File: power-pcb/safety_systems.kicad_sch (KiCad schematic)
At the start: 54 parts, among them J12 Conn_01x06, J13 Conn_01x03, J14 Conn_01x05, J15 Conn_01x02, J16 Conn_01x06, J17 Screw_Terminal_01x04, J18 Screw_Terminal_01x02, K1 G5Q-1A, K2 G5Q-1A, Q1 AO3400A, Q2 AO3400A, Q3 AO3400A, U22 SN65HVD230, U23 74AHC1G08

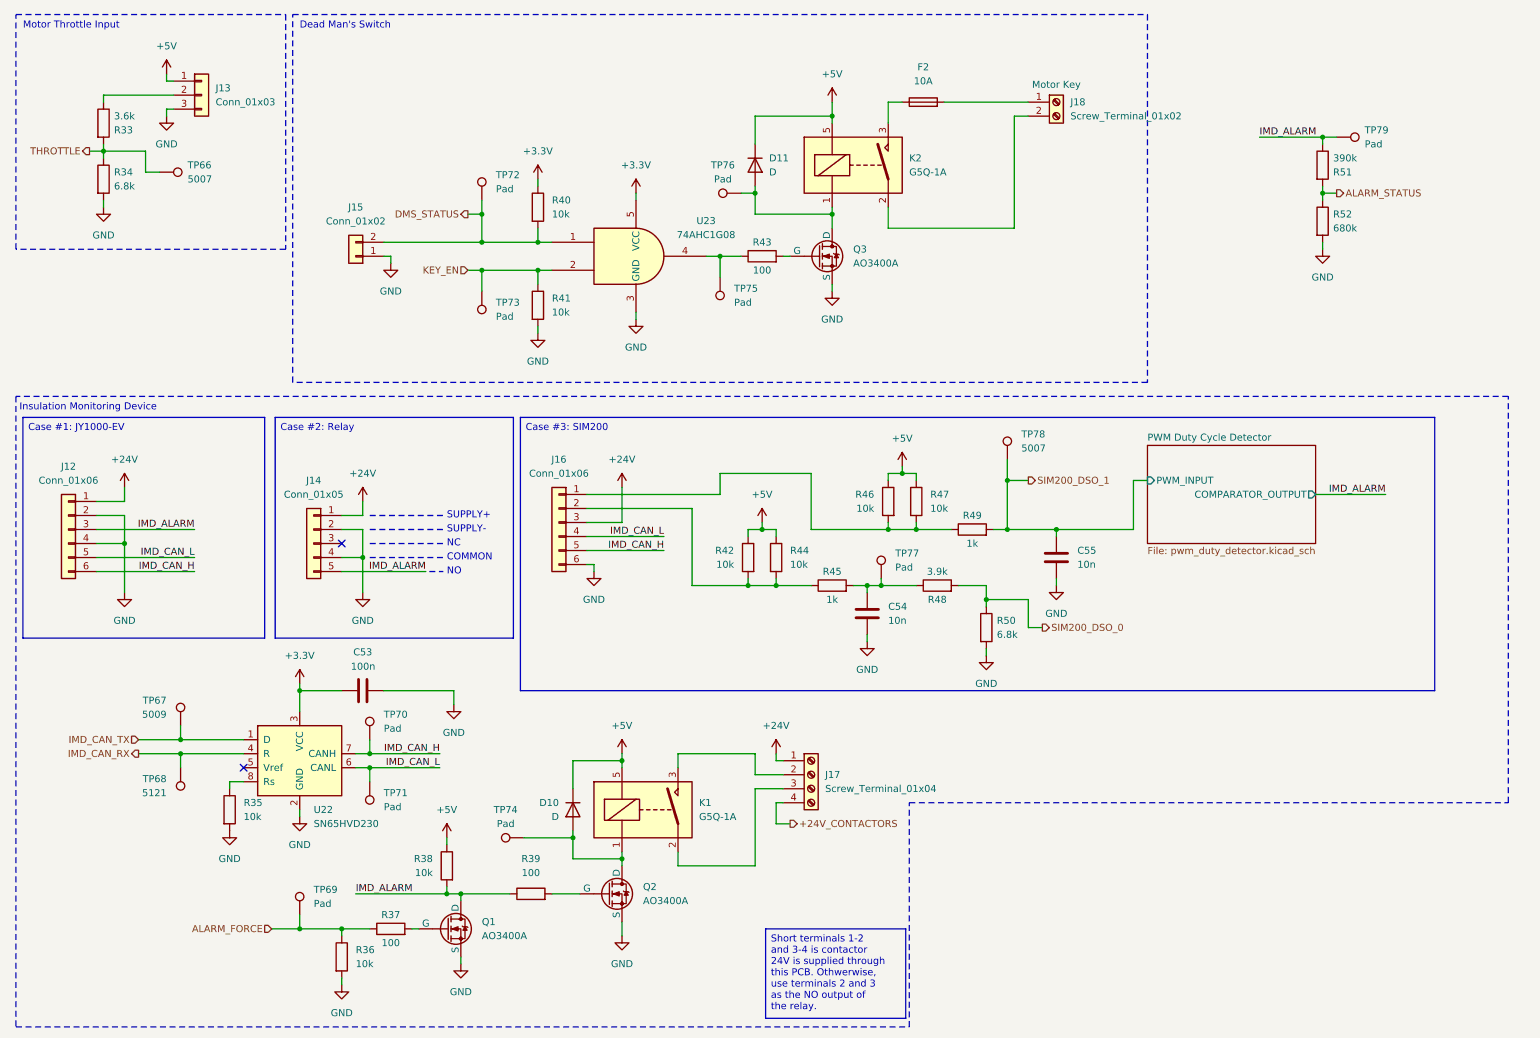
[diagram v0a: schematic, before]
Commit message: power-pcb: finish schematic pages 1 to 7
- overview
- non-isolated interfaces + power
- stm32 microcontroller
- relay board connection
- battery sensors
- 48v i-v sensing (x2)
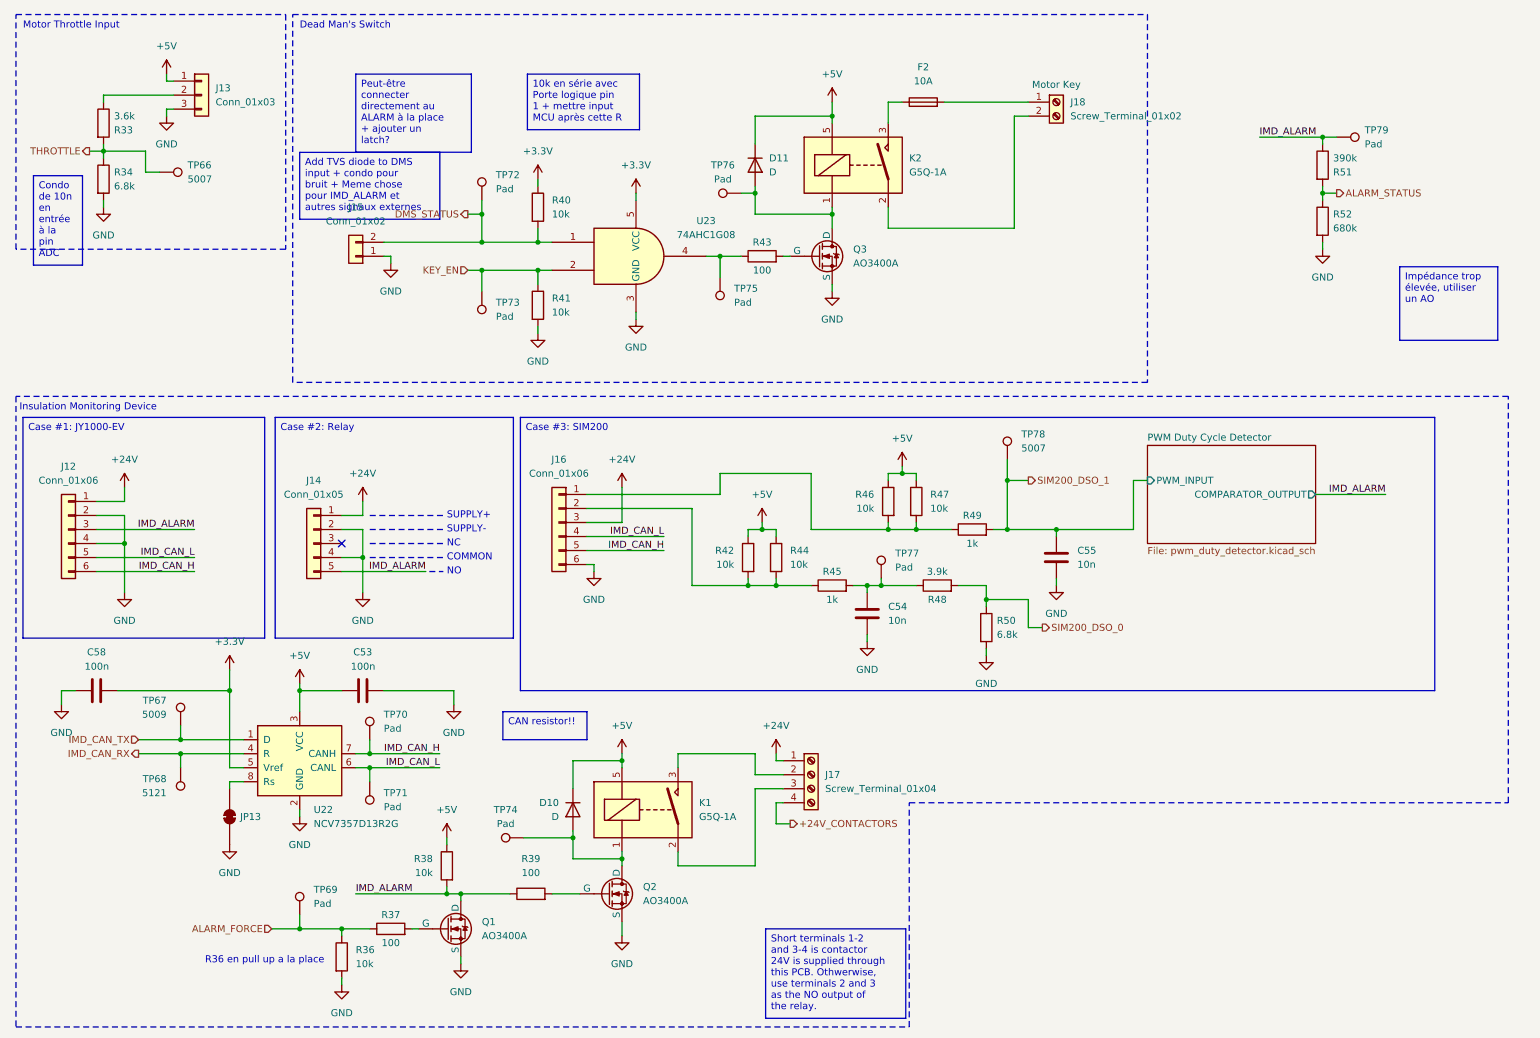
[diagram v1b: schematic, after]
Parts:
- removed R35: 10k, Resistor_SMD:R_0402_1005Metric, symbol Device:R
- added C58: 100n, Capacitor_SMD:C_0603_1608Metric_Pad1.08x0.95mm_HandSolder, symbol Device:C
- added JP13: SolderJumper_2_Bridged, symbol Jumper:SolderJumper_2_Bridged
- U22: value SN65HVD230 -> NCV7357D13R2G; JLCPCB C12084 -> C603987
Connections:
- net +3.3V: now also U22.5 (Vref), C58.1; no longer C53.2, U22.3 (VCC)
- net +5V: now also C53.2, U22.3 (VCC)
- net GND: now also C58.2, JP13.1 (A)
- net at U22.8 (Rs): now also JP13.2 (B)
- no-connect marks 2 -> 1
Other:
- note added: "R36 en pull up a la place"

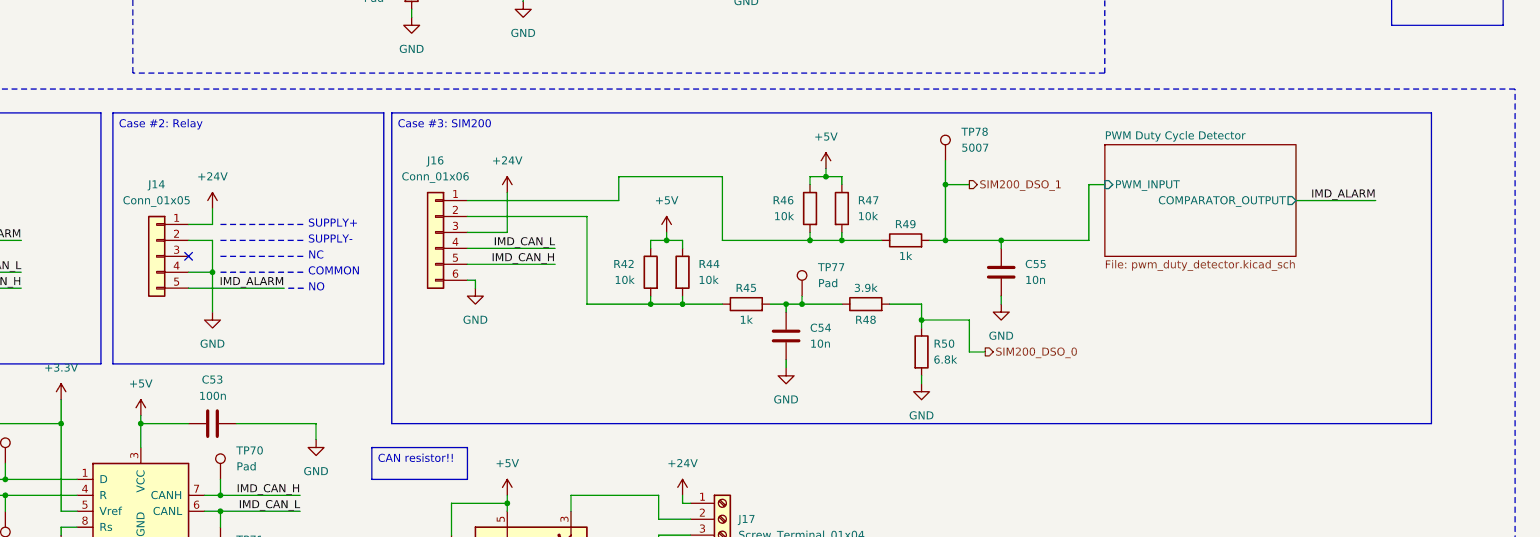
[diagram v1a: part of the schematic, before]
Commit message: power-pcb: remove unused sheets
After renaming, KiCad left the old sheets, but they were never
referenced.
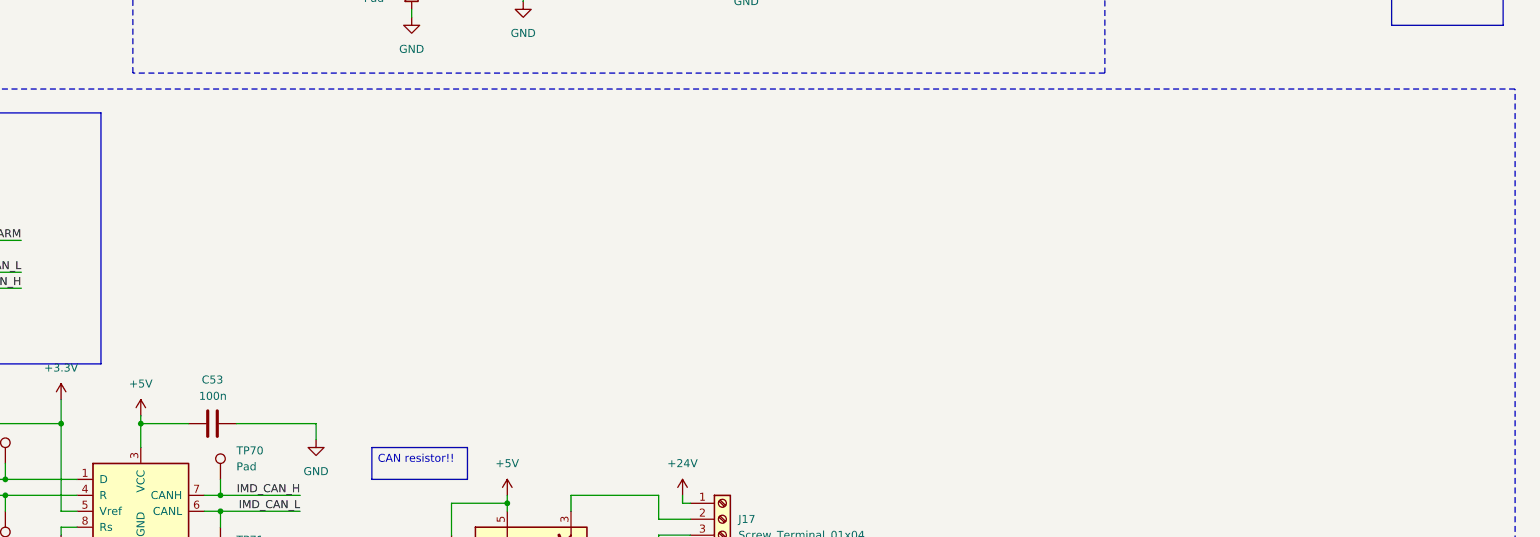
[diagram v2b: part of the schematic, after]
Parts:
- removed C54, C55: 10n, Capacitor_SMD:C_0603_1608Metric_Pad1.08x0.95mm_HandSolder, symbol Device:C
- removed J14: Conn_01x05, symbol Connector_Generic:Conn_01x05
- removed J16: Conn_01x06, symbol Connector_Generic:Conn_01x06
- removed R42, R44, R46, R47: 10k, symbol Device:R
- removed R45, R49: 1k, symbol Device:R
- removed R48: 3.9k, Resistor_SMD:R_0603_1608Metric, symbol Device:R
- removed R50: 6.8k, Resistor_SMD:R_0603_1608Metric, symbol Device:R
- removed TP77: Pad, symbol Connector:TestPoint
- removed TP78: 5007, symbol Connector:TestPoint
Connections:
- no-connect marks 1 -> 0
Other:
- removed sheet PWM Duty Cycle Detector
- note removed: "COMMON"
- note removed: "NC"
- note removed: "NO"
- note removed: "SUPPLY+"
- note removed: "SUPPLY-"
